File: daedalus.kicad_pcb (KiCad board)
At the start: 4 copper layers, 65 x 56.5 mm, 50 parts, among them J1 PWR, J2 Host, J3 IO Port, J4 MCU_I2C, J5 SWD, U3 MPU-6050, U4 W25Q128JVS, U5 MCU, U6 TPS56637, U7 AP2112K-3.3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

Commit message: fix raspberry pi hat pinout
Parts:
- moved G*** 0.32 mm to (123.6, 67.2)
- renumbered RST to SW1
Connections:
- J2 pad 1: (no net) -> +3V3
- J2 pad 17: unconnected-(J2-3V3-Pad17) -> +3V3
- J2 pad 4: unconnected-(J2-5V-Pad4) -> +5V
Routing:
- net /MCU/miso: track 58.8 -> 39.6 mm
- net /MCU/mosi: track 66.9 -> 55.7 mm
- net +3V3: track 49.1 -> 57.8 mm, vias 10 -> 11
- net GND: track 66.5 -> 59.0 mm, vias 20 -> 16
- net Net-(J2-GPCLK1/GPIO05): track 70.4 -> 74.3 mm, vias 0 -> 1
- net /MCU/run: track 139.6 -> 135.7 mm
- net Net-(J2-GPCLK0/GPIO04): track 54.8 -> 51.4 mm
- net Net-(J2-SCLK_SPI0/GPIO11): track 72.9 -> 70.1 mm
- net Net-(J2-MISO_SPI0/GPIO09): track 59.9 -> 57.3 mm
- net /MCU/uart_tx: track 39.1 -> 41.7 mm
- net Net-(J2-~{CE1}_SPI0/GPIO07): track 57.7 -> 60.2 mm
- net Net-(J2-MOSI_SPI0/GPIO10): track 52.6 -> 50.1 mm
- net /MCU/cs: track 37.4 -> 40.0 mm
- net Net-(J2-~{CE0}_SPI0/GPIO08): track 56.2 -> 58.8 mm
- net /MCU/uart_rx: track 40.3 -> 42.9 mm
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
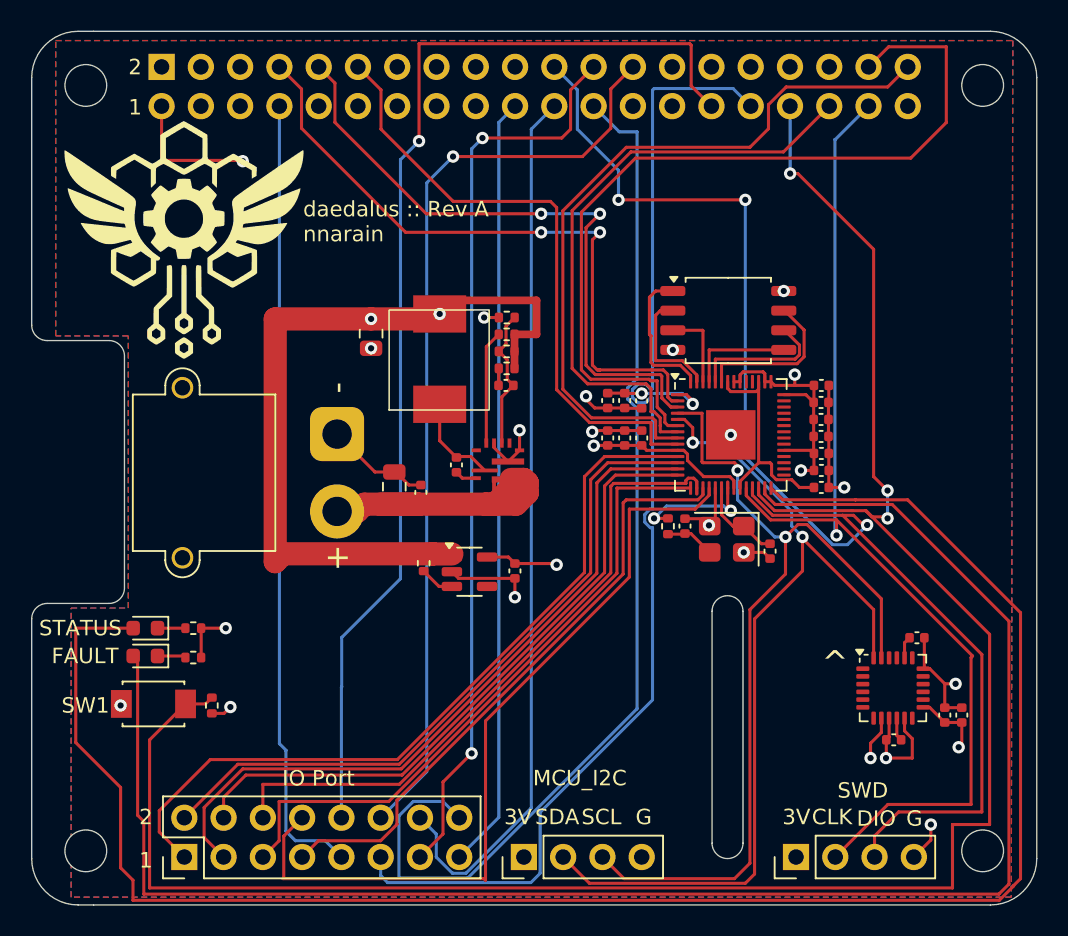
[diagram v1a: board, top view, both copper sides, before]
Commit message: Add power supply test points
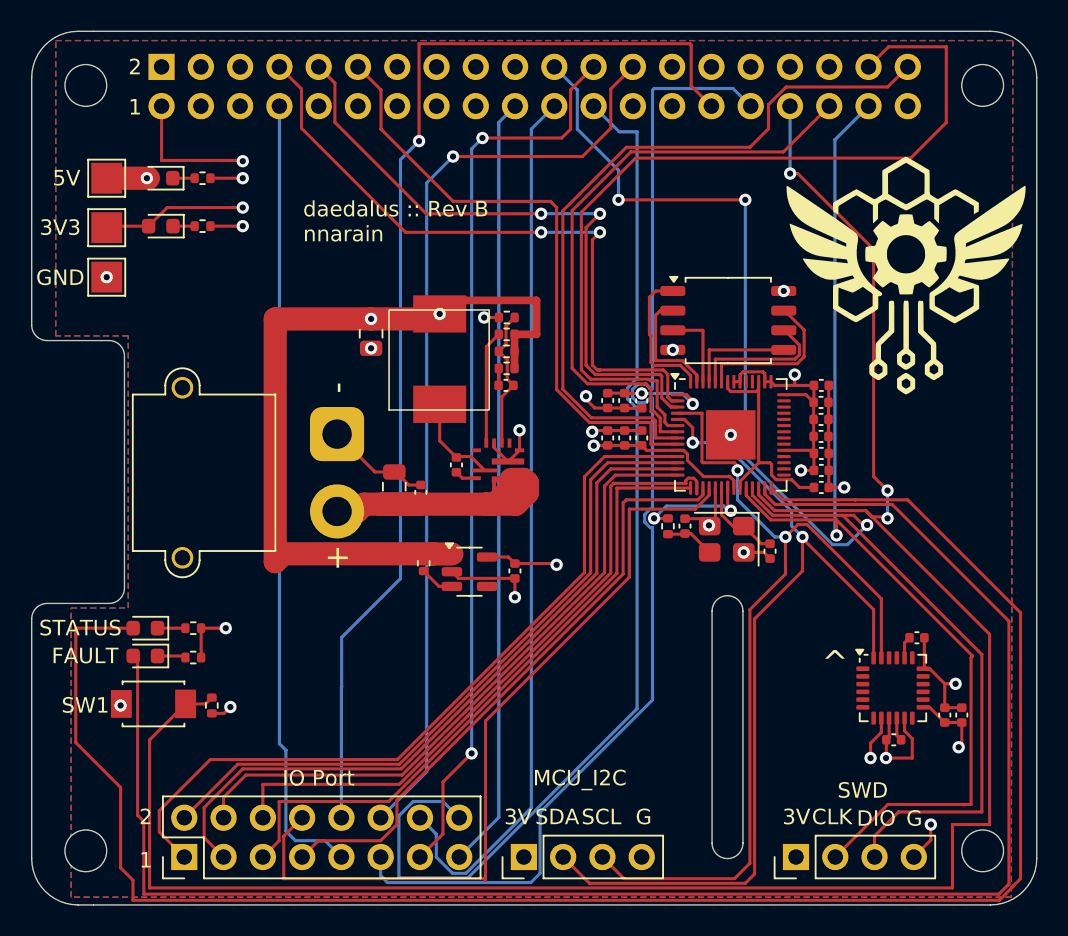
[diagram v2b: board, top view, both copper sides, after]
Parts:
- added 3V3: TP_3V3, TestPoint:TestPoint_Pad_2.0x2.0mm, F.Cu at (118.6, 66.3)
- added 5V: TP_5V, TestPoint:TestPoint_Pad_2.0x2.0mm, F.Cu at (118.6, 63.1)
- added D3: 3V3, LED_SMD:LED_0603_1608Metric, F.Cu at (122.1, 66.2)
- added D4: 5V, LED_SMD:LED_0603_1608Metric, F.Cu at (122.1, 63.1)
- added GND: TP_GND, TestPoint:TestPoint_Pad_2.0x2.0mm, F.Cu at (118.6, 69.5)
- added R6: 1k, Resistor_SMD:R_0402_1005Metric, F.Cu at (124.8, 63.1)
- added R7: 1k, Resistor_SMD:R_0402_1005Metric, F.Cu at (124.8, 66.2)
- moved G*** 46.8 mm to (170.3, 69.5)
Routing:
- net +3V3: track 57.8 -> 67.2 mm, vias 11 -> 12
- net GND: track 59.0 -> 63.1 mm, vias 16 -> 19
- net +5V: track 50.6 -> 53.3 mm, vias 2 -> 3
- net Net-(D4-K): track 0.00 -> 1.42 mm
- net Net-(D3-K): track 0.00 -> 1.40 mm
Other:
- board text added: "daedalus :: Rev ${REVISION} nnarain"
- board text removed: "daedalus :: Rev A nnarain"

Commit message: Switch to vertical xt30 connector
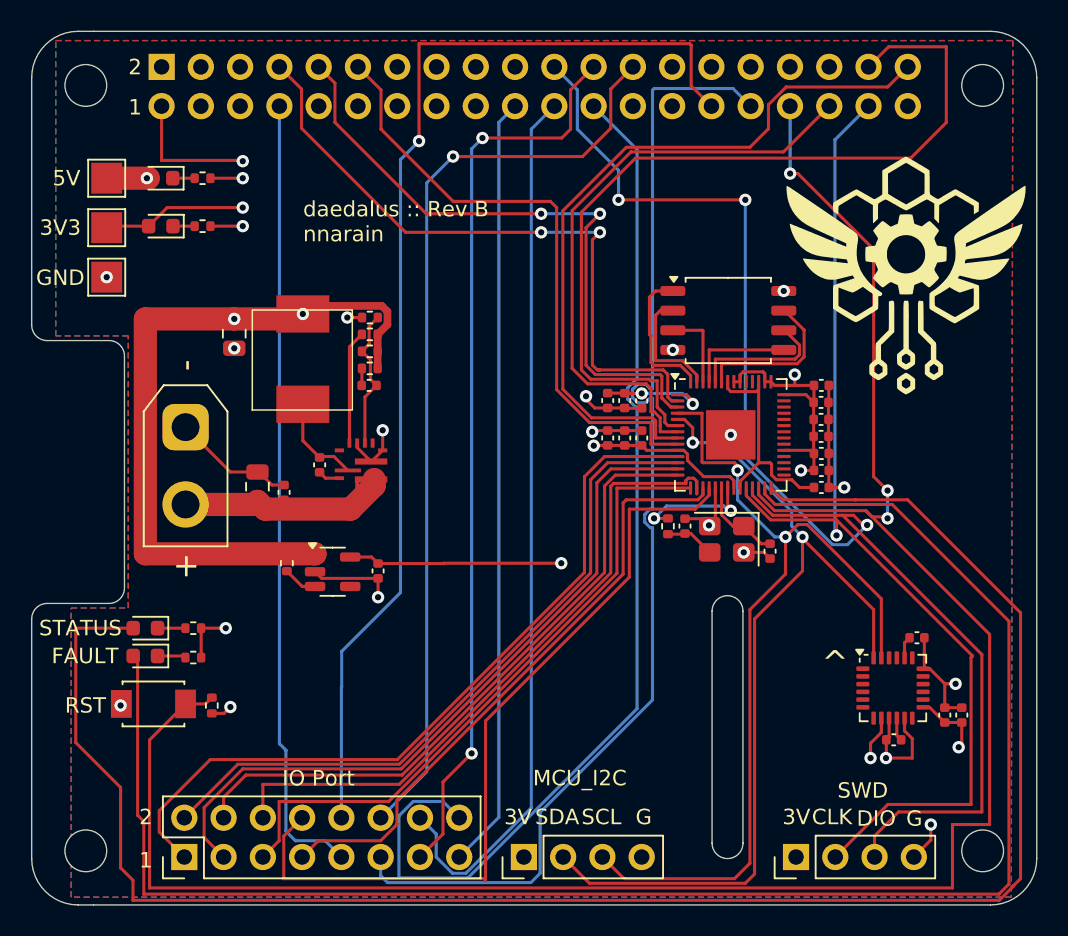
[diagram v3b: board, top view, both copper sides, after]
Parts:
- J1: footprint Connector_AMASS:AMASS_XT30PW-M_1x02_P2.50mm_Horizontal -> Connector_AMASS:AMASS_XT30UPB-M_1x02_P5.0mm_Vertical
- moved J1 9.81 mm to (123.7, 79.2), turned to -90 degrees
- moved C6 8.85 mm to (128.4, 83.0)
- moved C7 8.85 mm to (130.1, 83.4)
- moved C8 8.85 mm to (136.2, 88.5)
- moved Cboot1 8.85 mm to (132.4, 81.6)
- moved Cff1 8.85 mm to (135.6, 76.5)
- moved L2 8.85 mm to (131.3, 77.7)
- moved R3 8.85 mm to (130.3, 88.0)
- moved Rfbb1 8.85 mm to (135.6, 72.1)
- moved Rfbt1 8.85 mm to (135.6, 74.3)
- moved Rff1 8.85 mm to (135.6, 75.4)
- moved Rpg1 8.85 mm to (135.6, 73.2)
- moved U6 8.85 mm to (140.0, 81.9)
- moved U7 8.85 mm to (133.2, 88.5)
- moved Cout1 8.85 mm to (126.9, 73.2)
- renumbered SW1 to RST
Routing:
- net +3V3: track 67.2 -> 76.2 mm
- net /power_supply/pwr_vcc: track 20.3 -> 13.5 mm
- net +5V: track 53.3 -> 50.2 mm
- net GND: track 63.1 -> 64.1 mm
- net Net-(J2-SCLK_SPI0/GPIO11): track 70.1 -> 69.4 mm
